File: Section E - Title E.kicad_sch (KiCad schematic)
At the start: 6 parts, among them J10 Conn_01x03_Socket, J12 Conn_01x02_Socket, J13 Conn_01x03_Socket, J14 Conn_01x04_Socket, J15 Conn_01x03_Socket, J3 Conn_01x07_Socket

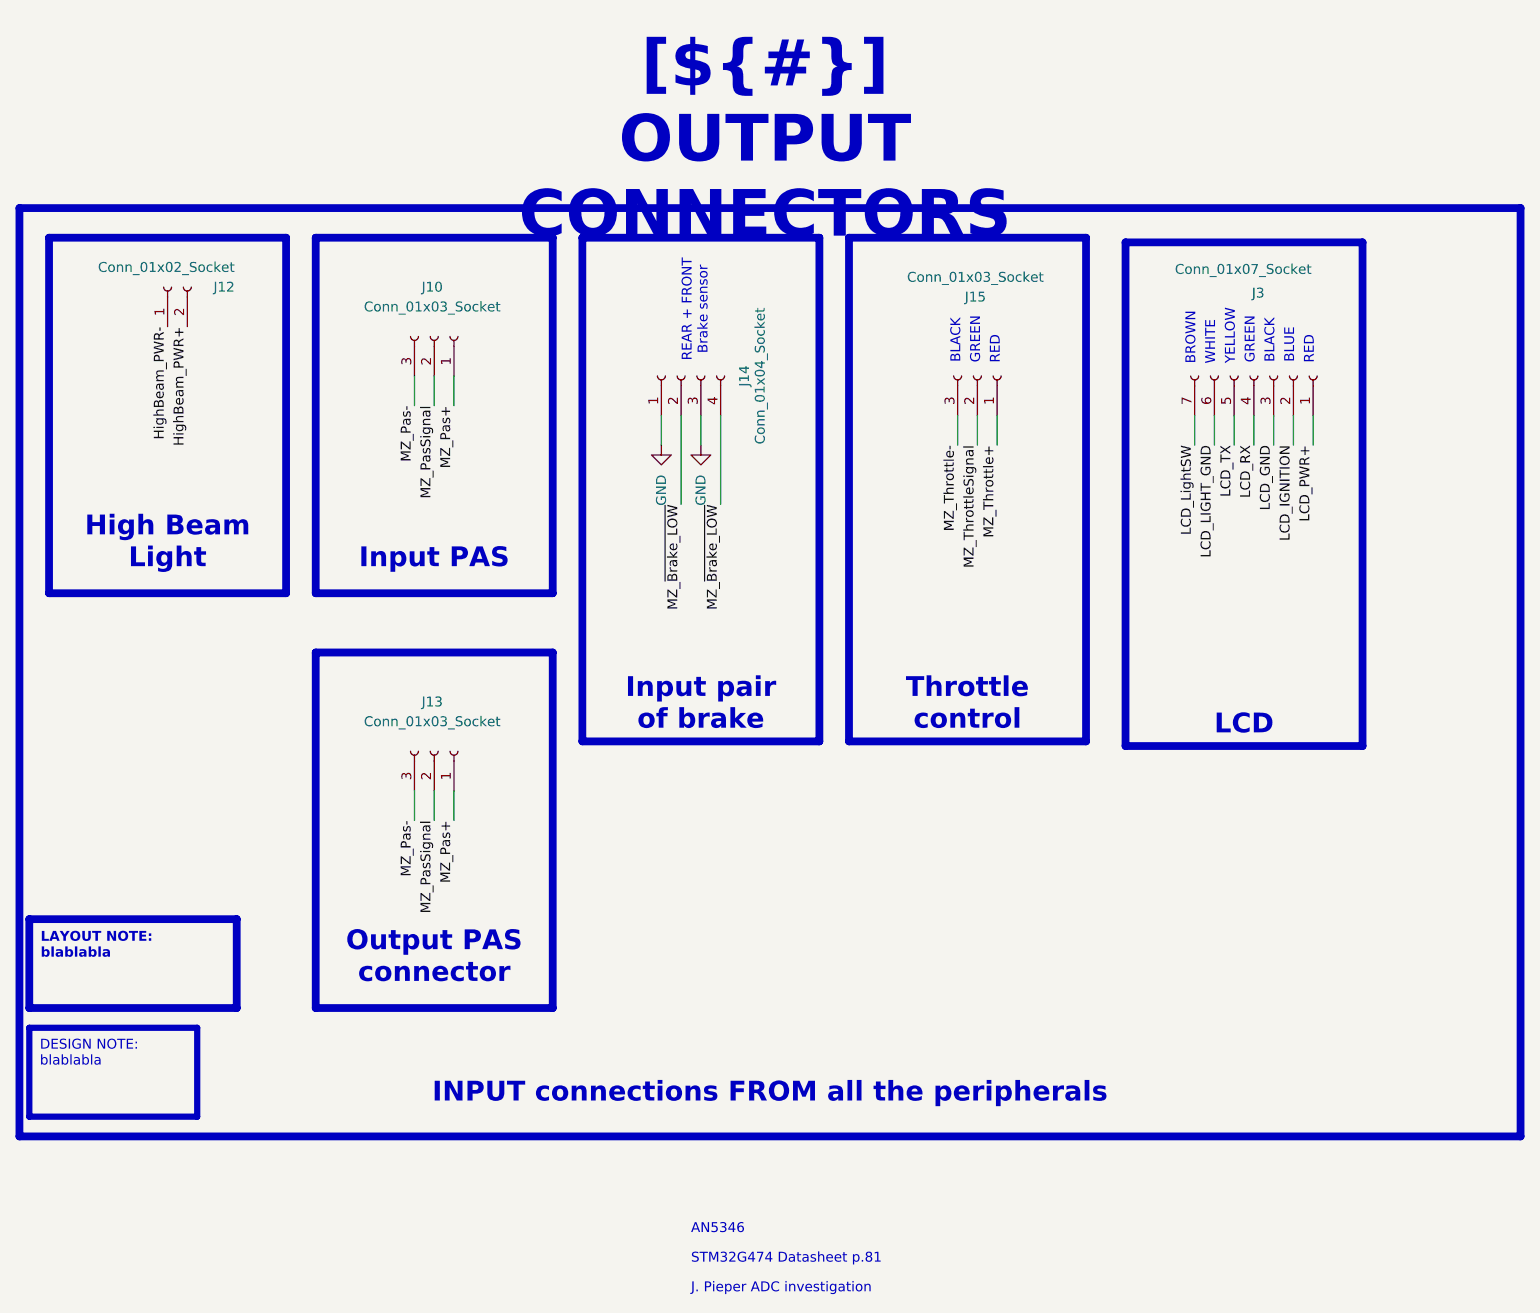
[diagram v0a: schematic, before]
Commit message: [SCHEMATICS] Ajout de convertisseur + autres
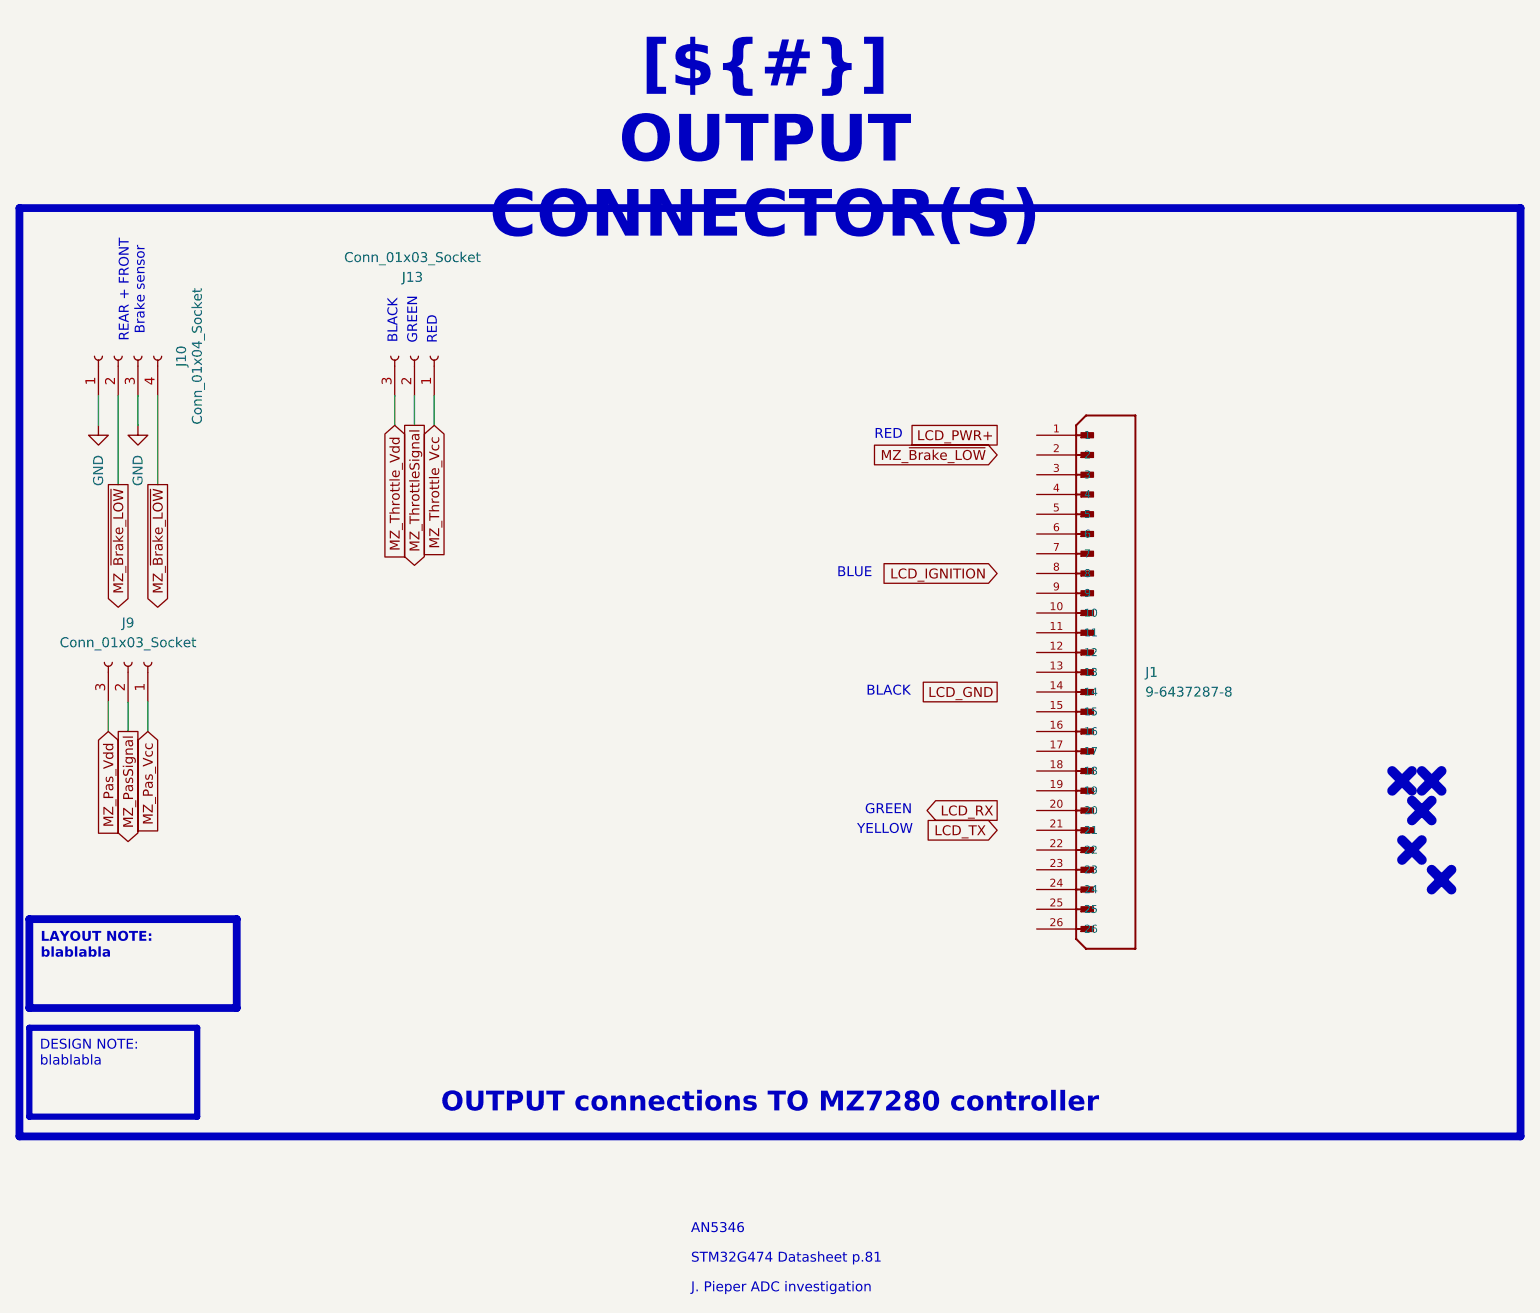
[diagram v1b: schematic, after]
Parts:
- removed J10, J15: Conn_01x03_Socket, symbol Connector:Conn_01x03_Socket
- removed J12: Conn_01x02_Socket, symbol Connector:Conn_01x02_Socket
- removed J14: Conn_01x04_Socket, symbol Connector:Conn_01x04_Socket
- removed J3: Conn_01x07_Socket, symbol Connector:Conn_01x07_Socket
- added J1: 9-6437287-8, LEGACY:TE_9-6437287-8, symbol LEGACY:9-6437287-8
- added J10: Conn_01x04_Socket, symbol Connector:Conn_01x04_Socket
- added J9: Conn_01x03_Socket, symbol Connector:Conn_01x03_Socket
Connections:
- net GND: now also J10.1 (Pin_1), J10.3 (Pin_3)
- net MZ_PasSignal: now also J9.2 (Pin_2); no longer J13.2 (Pin_2)
- net MZ_ThrottleSignal: now also J13.2 (Pin_2)
- net MZ_~{Brake_LOW}: now also J10.2 (Pin_2), J10.4 (Pin_4)
- net MZ_Pas+ renamed MZ_Throttle_Vcc
- net MZ_Pas- renamed MZ_Throttle_Vdd
- new net MZ_Pas_Vcc: J9.1 (Pin_1)
- new net MZ_Pas_Vdd: J9.3 (Pin_3)
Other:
- note removed: "BROWN"
- note removed: "WHITE"
- title: OUTPUT CONNECTORS -> OUTPUT CONNECTOR(S)
